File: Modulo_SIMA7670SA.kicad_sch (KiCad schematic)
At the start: 57 parts, among them J1 TBP01R1-508-02BE, J2 DB9 Hembra Impreso 90°, J3 U.FL IPEX1 MALE, J4 SMA-J-P-X-RA-TH1, J5 Jack DC 2.1mm PCB recto, Q1 BSS138, Q2 FDN340P, Q3 FDN340P, Q4 BSS138, U1 MAX232, U2 24LC512, U3 BKP-A7670SA (Módulo SIMCOM), U5 Black_Pill_STM32F411CEUx, U6 LM2596S_Modulo_Regulable, U7 LM7805_TO220

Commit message: Backup de rutina. Se modificaron pequeñas cosas en el esquema eléctrico.
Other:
- note added: "ST-LINK V2 (20070241) Black Pill (60069229)"
- note removed: "Cortar Diodo USB blackPill."
- note removed: "ST-LINK V2 (20070241) Black Pill (60069228)"
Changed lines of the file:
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@@
 		(company "E.Y.S.E. Equipos y Sistemas Electronicos S.A.C.I.")
 	)
-	(text "ST-LINK V2 (20070241)\nBlack Pill (60069228)"
+	(text "ST-LINK V2 (20070241)\nBlack Pill (60069229)"
 		(exclude_from_sim no)
 		(at 15.494 14.732 0)
@@
 	(text "Cable coaxial Pigtail\nRF-RG178, IPX U.FL a IPX U.FL"
 		(exclude_from_sim no)
-		(at 221.488 17.272 0)
+		(at 219.71 60.325 0)
 		(effects
 			(font
@@
 		)
 	)
-	(text "Cortar Diodo USB blackPill."
-		(exclude_from_sim no)
-		(at 121.285 174.625 0)
-		(effects
-			(font
-				(size 2.54 2.54)
-			)
-			(justify left)
-		)
-	)

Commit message: Se hicieron los arreglos para hacer funcionar el visor 3D de kicad 10.0.3. Comenzamos a tirar las primeras líneas del Gabinete basándonos en el modelo 3D.
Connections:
- net +12V: now also J1.1; no longer J1.2
- net GND: now also J1.2; no longer J1.1
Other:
- moved on the sheet: J1

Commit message: Rediseño HW: separación de dominios de alimentación y actualización de footprints - Riel 12V/5V del modem independiente (12V_StepDown→FDN340P→5V_MODEM): brownout resuelto y validado en PCB - Switches BC327/BC547 → topología FDN340P; MV5439A sustituido por WP59EGW/CA - Footprints en Damian_PCB: BKP-A7670SA, MF-NSMF005/60X, SM15-02HTG; corregido tamaño de pads del barrel jack - RS232: modificaciones incorporadas al esquema (pendiente pasar a PCB)
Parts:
- removed C1, C2, C3, C4: 10uF, Capacitor_THT:CP_Radial_D5.0mm_P2.00mm, symbol Device:C_Polarized
- added C1, C2, C3, C4: 100nF, Capacitor_THT:C_Disc_D5.0mm_W2.5mm_P2.50mm, symbol Device:C
- added D1, D4: SM15-02HTG, Damian_PCB:SM15-02HTG TSOT-23, symbol Power_Protection:RCLAMP0582B
- added F1: MF-NSMF005/60X, Damian_PCB:MF-NSMF005_60X, symbol Device:Polyfuse
- added R19, R20: 47, Resistor_SMD:R_0805_2012Metric, symbol Device:R
- D2, D3: value MV5439A -> WP59EGW/CA
- U1: value MAX232 -> MAX3232E
- U3: footprint Damian_PCB:SimCom_A7670SA -> Damian_PCB:BKP_A7670SA
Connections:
- net +5V_b: now also C3.2, F1.2; no longer C5.1, U1.16 (VCC)
- net GND: now also C4.2, D1.1 (K1), D4.1 (K1)
- net at J2.2: now also D4.2 (K2), R19.1; no longer U1.14 (T1OUT)
- net at J2.3: now also D1.2 (K2), R20.1; no longer U1.13 (R1IN)
- net at U1.6 (VS-): now also C4.1
- net at U1.2 (VS+): now also C3.1
- net at U1.1 (C1+): now also C1.1
- net at U1.3 (C1-): now also C1.2
- net at U1.4 (C2+): now also C2.1
- net at U1.5 (C2-): now also C2.2
- new net: R19.2, U1.14 (T1OUT)
- new net: R20.2, U1.13 (R1IN)
- new net: C5.1, F1.1, U1.16 (VCC)
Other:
- note added: "Ajustar el Regulador Voltaje a 5V. Luego se coloca el JP2"
- note added: "RS232 cable derecho."
- note removed: "Ajustar el Regulador Voltaje a 5V. Luego se coloca el JP6"
- moved on the sheet: JP4, Q1, Q2, R4, R5, R6, R7

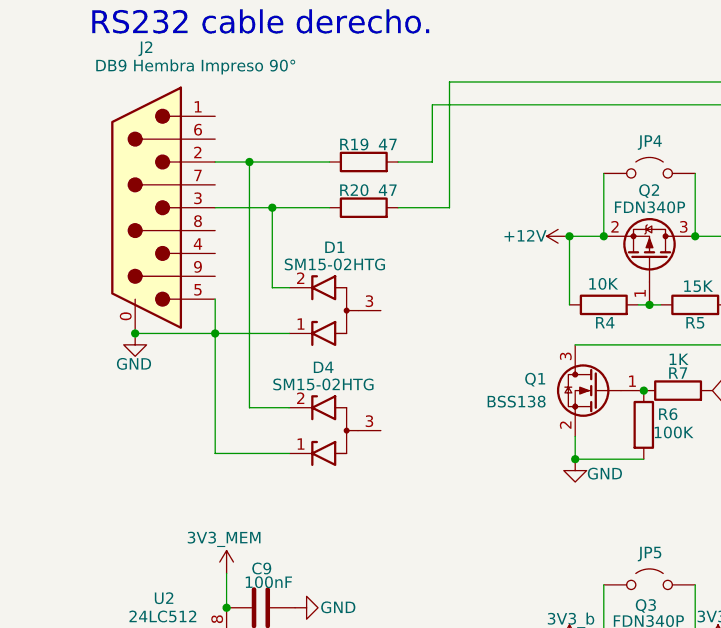
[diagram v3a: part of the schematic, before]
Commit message: Layout PCB completo: ruteo finalizado + archivos de fabricación
- Ruteo del PCB terminado (incluye modificaciones de RS232 pasadas del esquema al layout)
- Generados Gerber files y drill (Excellon) para fabricación
- Incorpora rieles de alimentación separados (dominio modem independiente) y footprints actualizados en Damian_PCB
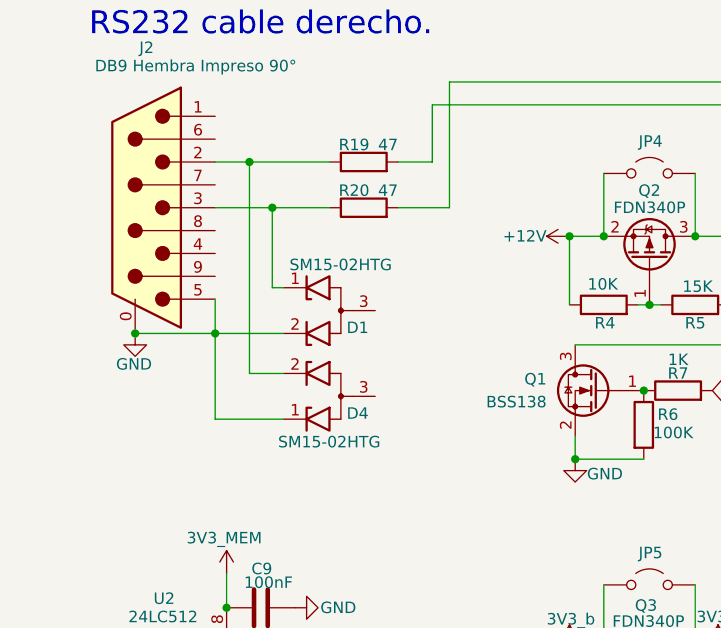
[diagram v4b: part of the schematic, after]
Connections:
- net GND: now also D1.2 (K2); no longer D1.1 (K1)
- net at J2.3, R20.1: now also D1.1 (K1); no longer D1.2 (K2)
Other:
- moved on the sheet: D1, D4
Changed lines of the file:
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@@
 	(wire
 		(pts
-			(xy 31.75 133.985) (xy 31.75 120.65)
+			(xy 31.75 120.65) (xy 39.37 120.65)
 		)
 		(stroke
@@
 	(wire
 		(pts
+			(xy 38.1 115.57) (xy 39.37 115.57)
+		)
+		(stroke
+			(width 0)
+			(type default)
+		)
+	)
+	(wire
+		(pts
 			(xy 213.995 51.435) (xy 217.805 51.435)
 		)
@@
 	(wire
 		(pts
-			(xy 40.005 128.905) (xy 35.56 128.905)
-		)
-		(stroke
-			(width 0)
-			(type default)
-		)
-	)
-	(wire
-		(pts
 			(xy 40.005 33.02) (xy 40.005 34.29)
 		)
@@
 	(wire
 		(pts
-			(xy 40.005 115.57) (xy 38.1 115.57)
+			(xy 74.93 102.87) (xy 74.93 109.855)
 		)
 		(stroke
@@
 	(wire
 		(pts
-			(xy 74.93 102.87) (xy 74.93 109.855)
+			(xy 31.75 120.65) (xy 31.75 130.175)
 		)
 		(stroke
@@
 	(wire
 		(pts
-			(xy 186.69 102.87) (xy 192.405 102.87)
+			(xy 31.75 130.175) (xy 39.37 130.175)
 		)
 		(stroke
@@
 	(wire
 		(pts
-			(xy 193.675 47.625) (xy 202.565 47.625)
+			(xy 186.69 102.87) (xy 192.405 102.87)
 		)
 		(stroke
@@
 	(wire
 		(pts
-			(xy 31.75 120.65) (xy 40.005 120.65)
+			(xy 193.675 47.625) (xy 202.565 47.625)
 		)
 		(stroke
@@
 	(wire
 		(pts
-			(xy 35.56 128.905) (xy 35.56 101.6)
+			(xy 35.56 125.095) (xy 39.37 125.095)
 		)
 		(stroke
@@
 	(wire
 		(pts
+			(xy 35.56 125.095) (xy 35.56 101.6)
+		)
+		(stroke
+			(width 0)
+			(type default)
+		)
+	)
+	(wire
+		(pts
 			(xy 71.12 177.165) (xy 71.12 179.705)
 		)
@@
 	(wire
 		(pts
-			(xy 40.005 133.985) (xy 31.75 133.985)
-		)
-		(stroke
-			(width 0)
-			(type default)
-		)
-	)
-	(wire
-		(pts
 			(xy 55.88 101.6) (xy 55.88 95.25)
 		)
@@
 	(symbol
 		(lib_id "Power_Protection:RCLAMP0582B")
-		(at 45.085 131.445 180)
+		(at 44.45 127.635 180)
 		(unit 1)
 		(body_style 1)
@@
 		(dnp no)
 		(property "Reference" "D4"
-			(at 42.545 124.46 0)
+			(at 46.355 129.54 0)
 			(show_name no)
 			(do_not_autoplace no)
@@
 		)
 		(property "Value" "SM15-02HTG"
-			(at 38.1 126.365 0)
+			(at 38.735 132.715 0)
 			(show_name no)
 			(do_not_autoplace no)
@@
 		)
 		(property "Footprint" "Damian_PCB:SM15-02HTG TSOT-23"
-			(at 45.085 123.825 0)
+			(at 44.45 120.015 0)
 			(hide yes)
 			(show_name no)
@@
 		)
 		(property "Datasheet" "https://www.semtech.com/products/circuit-protection/low-capacitance/rclamp0582b"
-			(at 43.815 133.985 0)
+			(at 43.18 130.175 0)
 			(hide yes)
 			(show_name no)
@@
 		)
 		(property "Description" "Low capacitance unidirectional dual ESD protection diode, SC-75"
-			(at 45.085 131.445 0)
+			(at 44.45 127.635 0)
 			(hide yes)
 			(show_name no)
@@
 	(symbol
 		(lib_id "Power_Protection:RCLAMP0582B")
-		(at 45.085 118.11 180)
+		(at 44.45 118.11 0)
+		(mirror y)
 		(unit 1)
 		(body_style 1)
@@
 		(dnp no)
 		(property "Reference" "D1"
-			(at 43.815 111.125 0)
+			(at 46.355 120.015 0)
 			(show_name no)
 			(do_not_autoplace no)
@@
 		)
 		(property "Value" "SM15-02HTG"
-			(at 39.37 113.03 0)
+			(at 40.005 113.03 0)
 			(show_name no)
 			(do_not_autoplace no)
@@
 		)
 		(property "Footprint" "Damian_PCB:SM15-02HTG TSOT-23"
-			(at 45.085 110.49 0)
+			(at 44.45 125.73 0)
 			(hide yes)
 			(show_name no)
@@
 		)
 		(property "Datasheet" "https://www.semtech.com/products/circuit-protection/low-capacitance/rclamp0582b"
-			(at 43.815 120.65 0)
+			(at 43.18 115.57 0)
 			(hide yes)
 			(show_name no)
@@
 		)
 		(property "Description" "Low capacitance unidirectional dual ESD protection diode, SC-75"
-			(at 45.085 118.11 0)
+			(at 44.45 118.11 0)
 			(hide yes)
 			(show_name no)

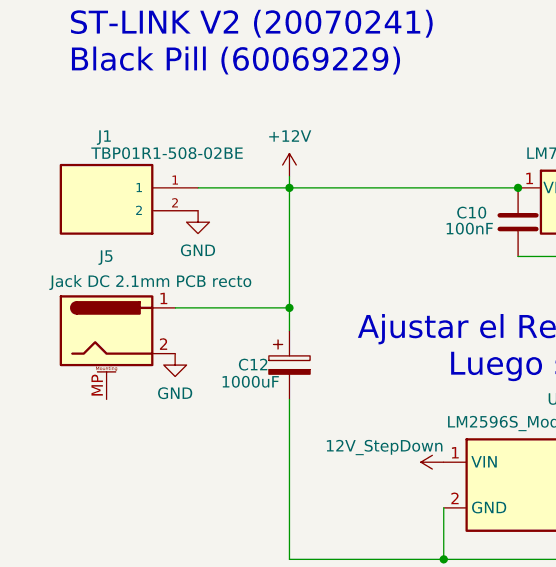
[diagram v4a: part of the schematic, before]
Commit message: Versión '2' del PCB ya terminada y los gerbers files listos para llevar al fabricante.
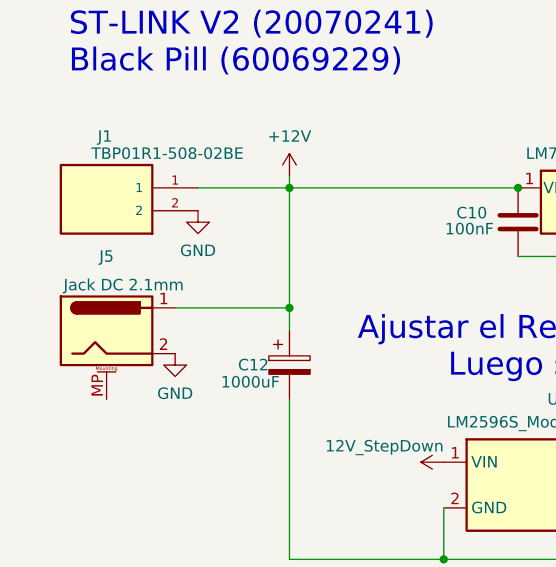
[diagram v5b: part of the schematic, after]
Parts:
- J5: value Jack DC 2.1mm PCB recto -> Jack DC 2.1mm
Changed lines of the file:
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@@
 			)
 		)
-		(property "Value" "Jack DC 2.1mm PCB recto"
-			(at 24.638 44.704 0)
+		(property "Value" "Jack DC 2.1mm"
+			(at 21.59 45.085 0)
 			(show_name no)
 			(do_not_autoplace no)
